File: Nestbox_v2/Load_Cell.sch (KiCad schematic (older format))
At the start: 33 parts, among them J601 LOAD_CELL_CONN_01X04, Q601 DMG2301L-7, Q602 DMG3402L, Q603 DMG2301L-7, Q604 DMG3402L, U601 ADS1220

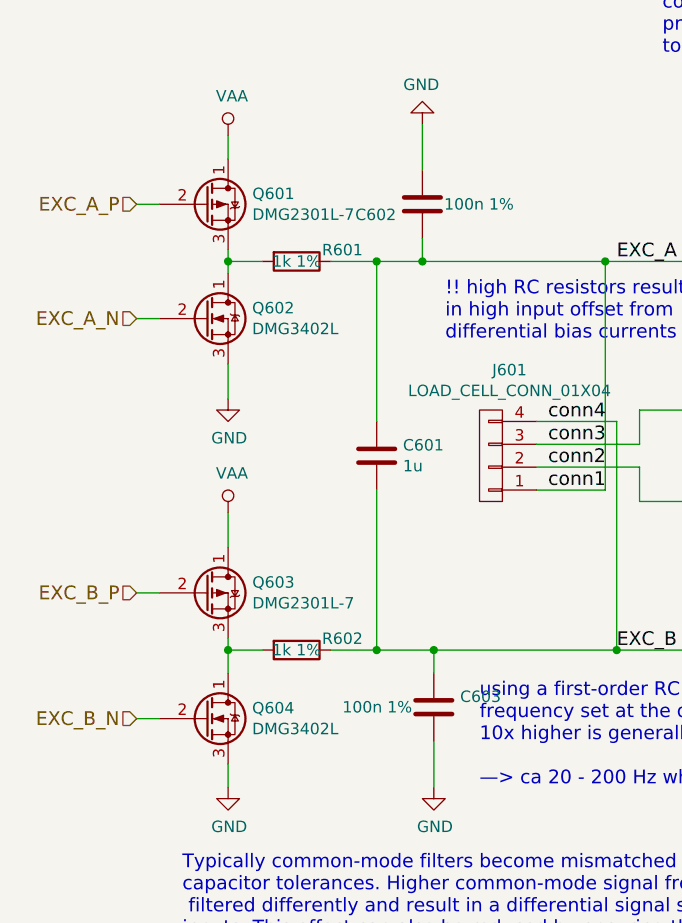
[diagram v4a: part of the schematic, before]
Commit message: corrected transistor pins
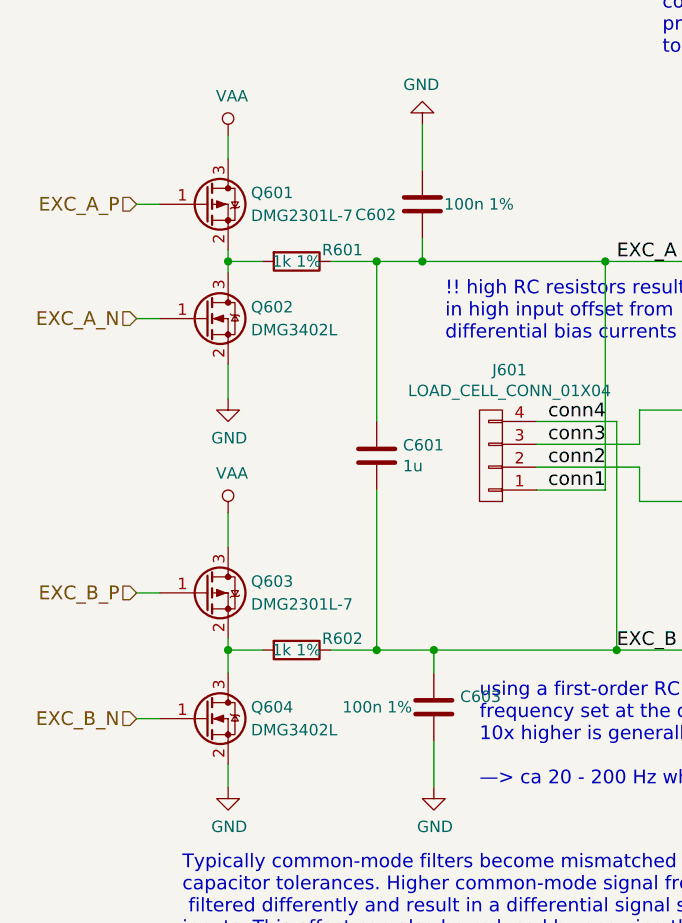
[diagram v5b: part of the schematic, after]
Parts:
- removed Q601, Q603: DMG2301L-7, TO_SOT_Packages_SMD:TSOT-23, symbol Q_PMOS_DGS
- removed Q602, Q604: DMG3402L, TO_SOT_Packages_SMD:TSOT-23, symbol Q_NMOS_DGS
- added Q601, Q603: DMG2301L-7, TO_SOT_Packages_SMD:TSOT-23, symbol Q_PMOS_GSD
- added Q602, Q604: DMG3402L, TO_SOT_Packages_SMD:TSOT-23, symbol Q_NMOS_GSD
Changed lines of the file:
@@
 $EndDescr
 $Comp
-L +3V3 #PWR051
+L +3V3 #PWR615
 U 1 1 5AF731D8
 P 7950 2900
-F 0 "#PWR051" H 7950 2750 50  0001 C CNN
+F 0 "#PWR615" H 7950 2750 50  0001 C CNN
 F 1 "+3V3" H 7965 3073 50  0000 C CNN
 F 2 "" H 7950 2900 50  0001 C CNN
@@
 $EndComp
 $Comp
-L GND #PWR052
+L GND #PWR616
 U 1 1 5AF734D9
 P 7950 4600
-F 0 "#PWR052" H 7950 4350 50  0001 C CNN
+F 0 "#PWR616" H 7950 4350 50  0001 C CNN
 F 1 "GND" H 7955 4427 50  0000 C CNN
 F 2 "" H 7950 4600 50  0001 C CNN
@@
 $EndComp
 $Comp
-L GND #PWR053
+L GND #PWR618
 U 1 1 5AF737C3
 P 8050 4600
-F 0 "#PWR053" H 8050 4350 50  0001 C CNN
+F 0 "#PWR618" H 8050 4350 50  0001 C CNN
 F 1 "GND" H 8055 4427 50  0000 C CNN
 F 2 "" H 8050 4600 50  0001 C CNN
@@
 $EndComp
 $Comp
-L GND #PWR054
+L GND #PWR619
 U 1 1 5AF737DA
 P 8650 3100
-F 0 "#PWR054" H 8650 2850 50  0001 C CNN
+F 0 "#PWR619" H 8650 2850 50  0001 C CNN
 F 1 "GND" V 8655 2972 50  0000 R CNN
 F 2 "" H 8650 3100 50  0001 C CNN
@@
 $EndComp
 $Comp
-L GND #PWR055
+L GND #PWR620
 U 1 1 5AF73803
 P 8650 3350
-F 0 "#PWR055" H 8650 3100 50  0001 C CNN
+F 0 "#PWR620" H 8650 3100 50  0001 C CNN
 F 1 "GND" V 8655 3222 50  0000 R CNN
 F 2 "" H 8650 3350 50  0001 C CNN
@@
 $EndComp
 $Comp
-L GND #PWR056
+L GND #PWR614
 U 1 1 5AF73B67
 P 7450 3400
-F 0 "#PWR056" H 7450 3150 50  0001 C CNN
+F 0 "#PWR614" H 7450 3150 50  0001 C CNN
 F 1 "GND" V 7455 3272 50  0000 R CNN
 F 2 "" H 7450 3400 50  0001 C CNN
@@
 $EndComp
 $Comp
-L GND #PWR057
+L GND #PWR613
 U 1 1 5AF73BBF
 P 7450 3100
-F 0 "#PWR057" H 7450 2850 50  0001 C CNN
+F 0 "#PWR613" H 7450 2850 50  0001 C CNN
 F 1 "GND" V 7455 2972 50  0000 R CNN
 F 2 "" H 7450 3100 50  0001 C CNN
@@
 $EndComp
 $Comp
-L GND #PWR058
+L GND #PWR610
 U 1 1 5AF756EC
 P 4400 4000
-F 0 "#PWR058" H 4400 3750 50  0001 C CNN
+F 0 "#PWR610" H 4400 3750 50  0001 C CNN
 F 1 "GND" H 4405 3827 50  0000 C CNN
 F 2 "" H 4400 4000 50  0001 C CNN
@@
 $EndComp
 $Comp
-L GND #PWR059
+L GND #PWR607
 U 1 1 5AF75761
 P 3900 4000
-F 0 "#PWR059" H 3900 3750 50  0001 C CNN
+F 0 "#PWR607" H 3900 3750 50  0001 C CNN
 F 1 "GND" H 3905 3827 50  0000 C CNN
 F 2 "" H 3900 4000 50  0001 C CNN
@@
 $EndComp
 $Comp
-L GND #PWR060
+L GND #PWR621
 U 1 1 5AF76892
 P 8800 4350
-F 0 "#PWR060" H 8800 4100 50  0001 C CNN
+F 0 "#PWR621" H 8800 4100 50  0001 C CNN
 F 1 "GND" H 8805 4177 50  0000 C CNN
 F 2 "" H 8800 4350 50  0001 C CNN
@@
 EXC_B
 $Comp
-L Q_NMOS_DGS Q602
-U 1 1 5AF89295
-P 1550 3400
-F 0 "Q602" H 1755 3446 50  0000 L CNN
-F 1 "DMG3402L" H 1755 3355 50  0000 L CNN
-F 2 "TO_SOT_Packages_SMD:TSOT-23" H 1750 3500 50  0001 C CNN
-F 3 "" H 1550 3400 50  0001 C CNN
-	1    1550 3400
-	1    0    0    -1
-$EndComp
-$Comp
-L Q_NMOS_DGS Q604
-U 1 1 5AF89446
-P 1550 5150
-F 0 "Q604" H 1755 5196 50  0000 L CNN
-F 1 "DMG3402L" H 1755 5105 50  0000 L CNN
-F 2 "TO_SOT_Packages_SMD:TSOT-23" H 1750 5250 50  0001 C CNN
-F 3 "" H 1550 5150 50  0001 C CNN
-	1    1550 5150
-	1    0    0    -1
-$EndComp
-$Comp
-L Q_PMOS_DGS Q603
-U 1 1 5AF89513
-P 1550 4600
-F 0 "Q603" H 1756 4646 50  0000 L CNN
-F 1 "DMG2301L-7" H 1756 4555 50  0000 L CNN
-F 2 "TO_SOT_Packages_SMD:TSOT-23" H 1750 4700 50  0001 C CNN
-F 3 "" H 1550 4600 50  0001 C CNN
-	1    1550 4600
-	1    0    0    -1
-$EndComp
-$Comp
-L Q_PMOS_DGS Q601
-U 1 1 5AF89674
-P 1550 2900
-F 0 "Q601" H 1756 2946 50  0000 L CNN
-F 1 "DMG2301L-7" H 1756 2855 50  0000 L CNN
-F 2 "TO_SOT_Packages_SMD:TSOT-23" H 1750 3000 50  0001 C CNN
-F 3 "" H 1550 2900 50  0001 C CNN
-	1    1550 2900
-	1    0    0    -1
-$EndComp
-$Comp
-L GND #PWR061
+L GND #PWR602
 U 1 1 5AF8B9E6
 P 1650 3750
-F 0 "#PWR061" H 1650 3500 50  0001 C CNN
+F 0 "#PWR602" H 1650 3500 50  0001 C CNN
 F 1 "GND" H 1655 3577 50  0000 C CNN
 F 2 "" H 1650 3750 50  0001 C CNN
@@
 $EndComp
 $Comp
-L GND #PWR062
+L GND #PWR604
 U 1 1 5AF8BA1F
 P 1650 5450
-F 0 "#PWR062" H 1650 5200 50  0001 C CNN
+F 0 "#PWR604" H 1650 5200 50  0001 C CNN
 F 1 "GND" H 1655 5277 50  0000 C CNN
 F 2 "" H 1650 5450 50  0001 C CNN
@@
 $EndComp
 $Comp
-L VAA #PWR063
+L VAA #PWR601
 U 1 1 5AF8BE8C
 P 1650 2600
-F 0 "#PWR063" H 1650 2450 50  0001 C CNN
+F 0 "#PWR601" H 1650 2450 50  0001 C CNN
 F 1 "VAA" H 1667 2773 50  0000 C CNN
 F 2 "" H 1650 2600 50  0001 C CNN
@@
 $EndComp
 $Comp
-L VAA #PWR064
+L VAA #PWR603
 U 1 1 5AF8C0F0
 P 1650 4250
-F 0 "#PWR064" H 1650 4100 50  0001 C CNN
+F 0 "#PWR603" H 1650 4100 50  0001 C CNN
 F 1 "VAA" H 1667 4423 50  0000 C CNN
 F 2 "" H 1650 4250 50  0001 C CNN
@@
 $EndComp
 $Comp
-L VAA #PWR065
+L VAA #PWR617
 U 1 1 5AF8C129
 P 8050 2550
-F 0 "#PWR065" H 8050 2400 50  0001 C CNN
+F 0 "#PWR617" H 8050 2400 50  0001 C CNN
 F 1 "VAA" H 8067 2723 50  0000 C CNN
 F 2 "" H 8050 2550 50  0001 C CNN
@@
 $EndComp
 $Comp
-L GND #PWR066
+L GND #PWR606
 U 1 1 5AF8D573
 P 2550 5450
-F 0 "#PWR066" H 2550 5200 50  0001 C CNN
+F 0 "#PWR606" H 2550 5200 50  0001 C CNN
 F 1 "GND" H 2555 5277 50  0000 C CNN
 F 2 "" H 2550 5450 50  0001 C CNN
@@
 $EndComp
 $Comp
-L GND #PWR067
+L GND #PWR605
 U 1 1 5AF8D7AF
 P 2500 2550
-F 0 "#PWR067" H 2500 2300 50  0001 C CNN
+F 0 "#PWR605" H 2500 2300 50  0001 C CNN
 F 1 "GND" H 2505 2377 50  0000 C CNN
 F 2 "" H 2500 2550 50  0001 C CNN
@@
 $EndComp
 $Comp
-L GND #PWR068
+L GND #PWR612
 U 1 1 5AF97D06
 P 6100 4000
-F 0 "#PWR068" H 6100 3750 50  0001 C CNN
+F 0 "#PWR612" H 6100 3750 50  0001 C CNN
 F 1 "GND" H 6105 3827 50  0000 C CNN
 F 2 "" H 6100 4000 50  0001 C CNN
@@
 $EndComp
 $Comp
-L GND #PWR069
+L GND #PWR611
 U 1 1 5AF97F53
 P 5600 4000
-F 0 "#PWR069" H 5600 3750 50  0001 C CNN
+F 0 "#PWR611" H 5600 3750 50  0001 C CNN
 F 1 "GND" H 5605 3827 50  0000 C CNN
 F 2 "" H 5600 4000 50  0001 C CNN
@@
 LIGHTBARRIER_LED_OUTPUT
 $Comp
-L +3.3V #PWR070
+L +3.3V #PWR608
 U 1 1 5B145174
 P 3950 6750
-F 0 "#PWR070" H 3950 6600 50  0001 C CNN
+F 0 "#PWR608" H 3950 6600 50  0001 C CNN
 F 1 "+3.3V" H 3950 6890 50  0000 C CNN
 F 2 "" H 3950 6750 50  0001 C CNN
@@
 $EndComp
 $Comp
-L GND #PWR071
+L GND #PWR609
 U 1 1 5B14520C
 P 3950 7050
-F 0 "#PWR071" H 3950 6800 50  0001 C CNN
+F 0 "#PWR609" H 3950 6800 50  0001 C CNN
 F 1 "GND" H 3950 6900 50  0000 C CNN
 F 2 "" H 3950 7050 50  0001 C CNN
@@
 Wire Wire Line
 	3300 4150 3300 3150
+$Comp
+L Q_PMOS_GSD Q603
+U 1 1 5B188D68
+P 1550 4600
+F 0 "Q603" H 1750 4650 50  0000 L CNN
+F 1 "DMG2301L-7" H 1750 4550 50  0000 L CNN
+F 2 "TO_SOT_Packages_SMD:TSOT-23" H 1750 4700 50  0001 C CNN
+F 3 "" H 1550 4600 50  0001 C CNN
+	1    1550 4600
+	1    0    0    -1
+$EndComp
+$Comp
+L Q_PMOS_GSD Q601
+U 1 1 5B1892D4
+P 1550 2900
+F 0 "Q601" H 1750 2950 50  0000 L CNN
+F 1 "DMG2301L-7" H 1750 2850 50  0000 L CNN
+F 2 "TO_SOT_Packages_SMD:TSOT-23" H 1750 3000 50  0001 C CNN
+F 3 "" H 1550 2900 50  0001 C CNN
+	1    1550 2900
+	1    0    0    -1
+$EndComp
+$Comp
+L Q_NMOS_GSD Q602
+U 1 1 5B1899A1
+P 1550 3400
+F 0 "Q602" H 1750 3450 50  0000 L CNN
+F 1 "DMG3402L" H 1750 3350 50  0000 L CNN
+F 2 "TO_SOT_Packages_SMD:TSOT-23" H 1750 3500 50  0001 C CNN
+F 3 "" H 1550 3400 50  0001 C CNN
+	1    1550 3400
+	1    0    0    -1
+$EndComp
+$Comp
+L Q_NMOS_GSD Q604
+U 1 1 5B189ECC
+P 1550 5150
+F 0 "Q604" H 1750 5200 50  0000 L CNN
+F 1 "DMG3402L" H 1750 5100 50  0000 L CNN
+F 2 "TO_SOT_Packages_SMD:TSOT-23" H 1750 5250 50  0001 C CNN
+F 3 "" H 1550 5150 50  0001 C CNN
+	1    1550 5150
+	1    0    0    -1
+$EndComp
 $EndSCHEMATC

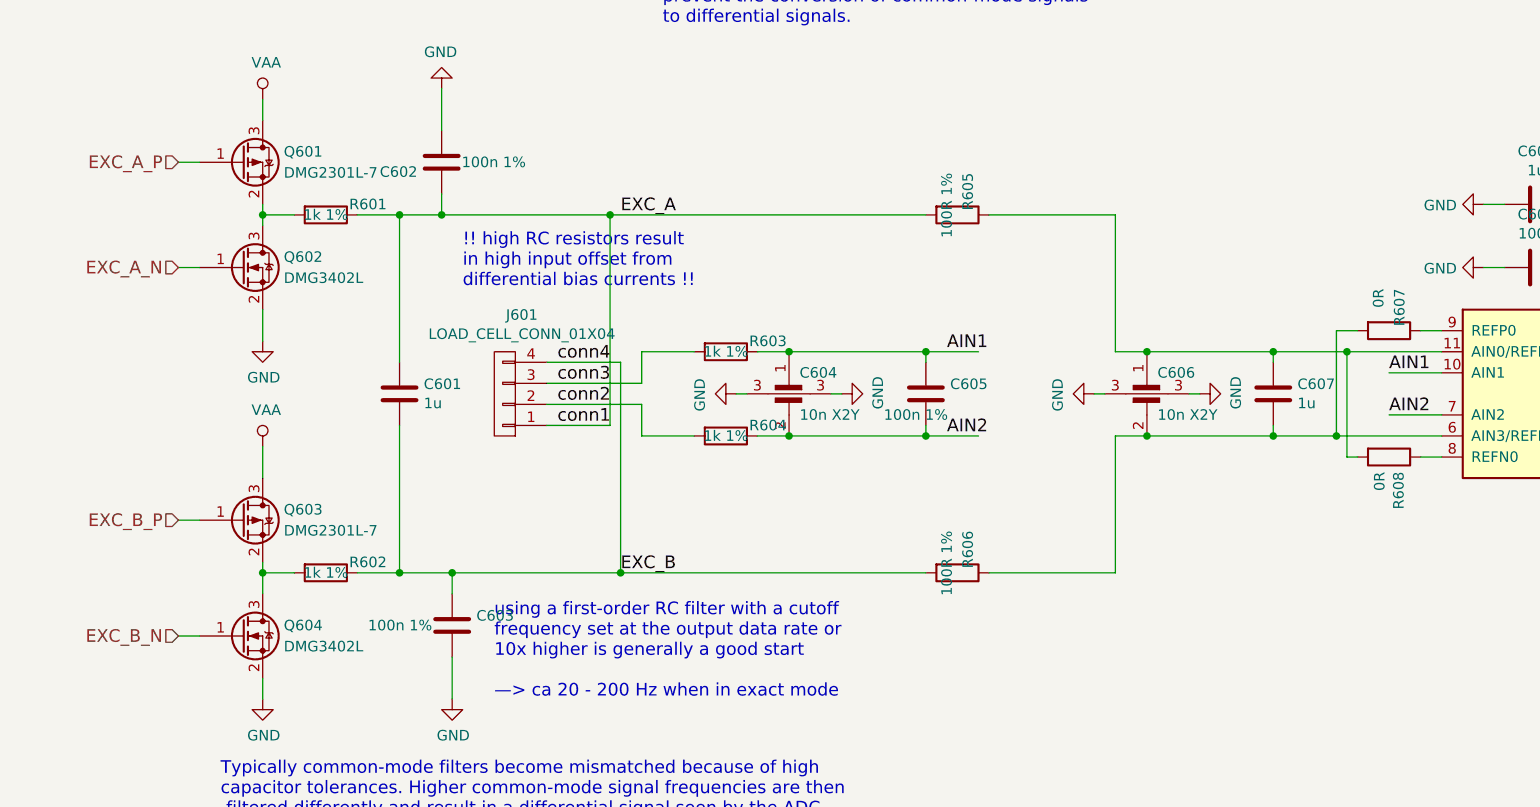
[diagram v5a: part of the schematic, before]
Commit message: annotated schematic with necessary changes to load cell circuit. added pull-ups for enable PMOSes
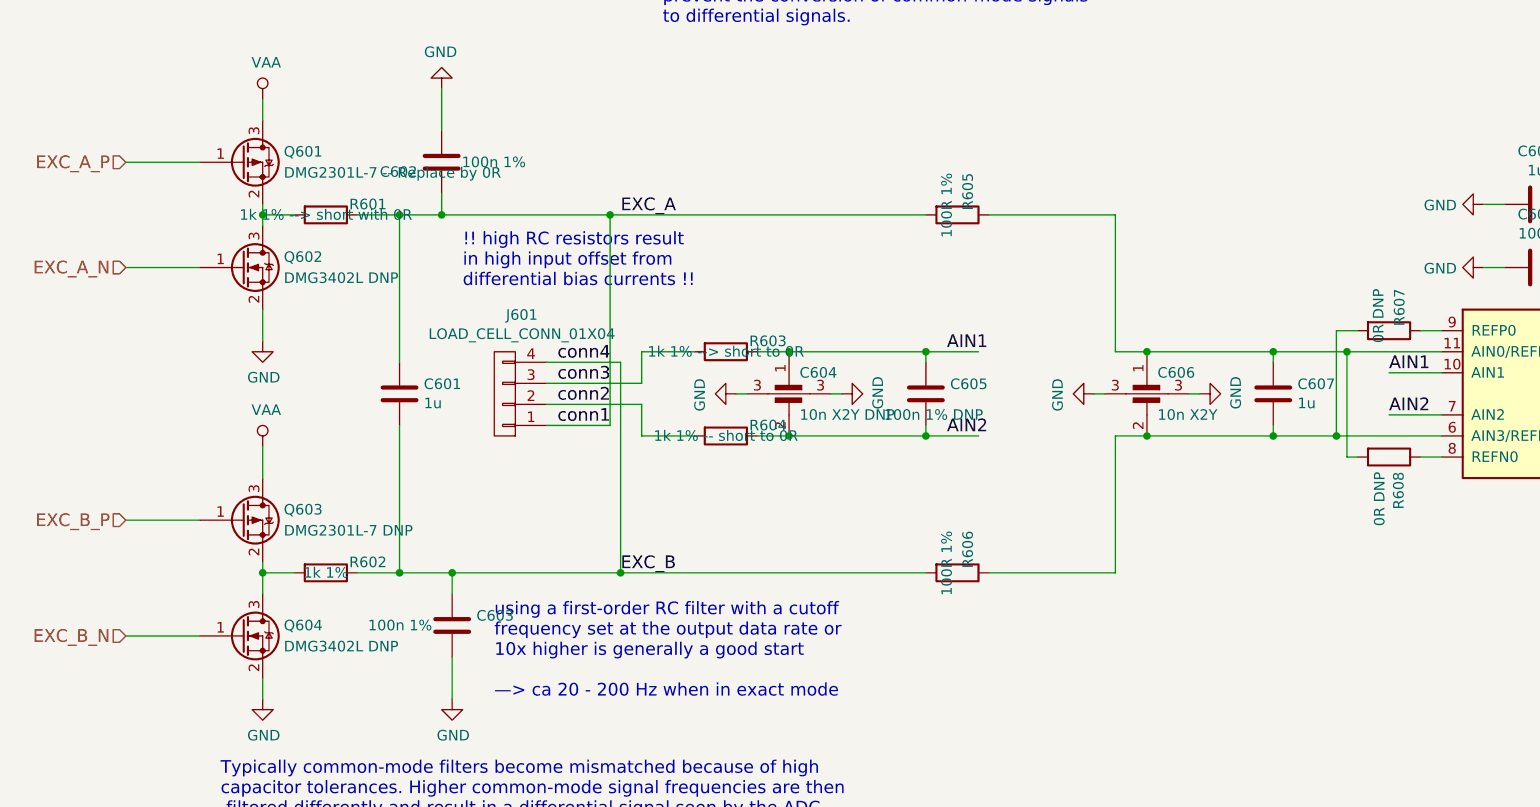
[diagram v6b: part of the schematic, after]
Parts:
- C604: value 10n X2Y -> 10n X2Y DNP
- C605: value 100n 1% -> 100n 1% DNP
- Q601: value DMG2301L-7 -> DMG2301L-7 -- Replace by 0R
- Q602, Q604: value DMG3402L -> DMG3402L DNP
- Q603: value DMG2301L-7 -> DMG2301L-7 DNP
- R601: value 1k 1% -> 1k 1% --> short with 0R
- R603: value 1k 1% -> 1k 1% --> short to 0R
- R604: value 1k 1% -> 1k 1% -- short to 0R
- R607, R608: value 0R -> 0R DNP
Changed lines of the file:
@@
 P 4800 4000
 F 0 "C605" H 4915 4046 50  0000 L CNN
-F 1 "100n 1%" H 4600 3900 50  0000 L CNN
+F 1 "100n 1% DNP" H 4600 3900 50  0000 L CNN
 F 2 "Capacitors_SMD:C_0603" H 4838 3850 50  0001 C CNN
 F 3 "" H 4800 4000 50  0001 C CNN
@@
 P 3850 3800
 F 0 "R603" V 3800 4000 50  0000 C CNN
-F 1 "1k 1%" V 3850 3800 50  0000 C CNN
+F 1 "1k 1% --> short to 0R" V 3850 3800 50  0000 C CNN
 F 2 "Resistors_SMD:R_0603" V 3780 3800 50  0001 C CNN
 F 3 "" H 3850 3800 50  0001 C CNN
@@
 P 3850 4200
 F 0 "R604" V 3800 4400 50  0000 C CNN
-F 1 "1k 1%" V 3850 4200 50  0000 C CNN
+F 1 "1k 1% -- short to 0R" V 3850 4200 50  0000 C CNN
 F 2 "Resistors_SMD:R_0603" V 3780 4200 50  0001 C CNN
 F 3 "" H 3850 4200 50  0001 C CNN
@@
 P 1950 3150
 F 0 "R601" V 1900 3350 50  0000 C CNN
-F 1 "1k 1%" V 1950 3150 50  0000 C CNN
+F 1 "1k 1% --> short with 0R" V 1950 3150 50  0000 C CNN
 F 2 "Resistors_SMD:R_0603" V 1880 3150 50  0001 C CNN
 F 3 "" H 1950 3150 50  0001 C CNN
@@
 P 7000 4300
 F 0 "R608" H 7070 4346 50  0000 L CNN
-F 1 "0R" H 7070 4255 50  0000 L CNN
+F 1 "0R DNP" H 7070 4255 50  0000 L CNN
 F 2 "Resistors_SMD:R_0603" V 6930 4300 50  0001 C CNN
 F 3 "" H 7000 4300 50  0001 C CNN
@@
 P 7000 3700
 F 0 "R607" H 6800 3750 50  0000 L CNN
-F 1 "0R" H 6800 3650 50  0000 L CNN
+F 1 "0R DNP" H 6800 3650 50  0000 L CNN
 F 2 "Resistors_SMD:R_0603" V 6930 3700 50  0001 C CNN
 F 3 "" H 7000 3700 50  0001 C CNN
@@
 P 4150 4100
 F 0 "C604" H 4200 4300 50  0000 L CNN
-F 1 "10n X2Y" H 4200 4100 50  0000 L CNN
+F 1 "10n X2Y DNP" H 4200 4100 50  0000 L CNN
 F 2 "Octanis3:Capacitor_X2Y_603" V 4150 4100 50  0001 C CNN
 F 3 "" V 4150 4100 50  0001 C CNN
@@
 Connection ~ 5850 4200
 Wire Wire Line
-	1250 3400 1350 3400
-Wire Wire Line
-	1250 2900 1350 2900
-Wire Wire Line
-	1250 4600 1350 4600
-Wire Wire Line
-	1250 5150 1350 5150
+	1000 3400 1350 3400
+Wire Wire Line
+	1000 2900 1350 2900
+Wire Wire Line
+	1000 4600 1350 4600
+Wire Wire Line
+	1000 5150 1350 5150
 Text HLabel 9750 3700 2    60   Input ~ 0
 SPI_SCK
@@
 Text HLabel 9750 4200 2    60   Input ~ 0
 DRDY_N
-Text HLabel 1250 2900 0    60   Input ~ 0
+Text HLabel 1000 2900 0    60   Input ~ 0
 EXC_A_P
-Text HLabel 1250 3400 0    60   Input ~ 0
+Text HLabel 1000 3400 0    60   Input ~ 0
 EXC_A_N
-Text HLabel 1250 5150 0    60   Input ~ 0
+Text HLabel 1000 5150 0    60   Input ~ 0
 EXC_B_N
-Text HLabel 1250 4600 0    60   Input ~ 0
+Text HLabel 1000 4600 0    60   Input ~ 0
 EXC_B_P
 Text Label 3050 4150 0    60   ~ 0
@@
 P 1550 4600
 F 0 "Q603" H 1750 4650 50  0000 L CNN
-F 1 "DMG2301L-7" H 1750 4550 50  0000 L CNN
+F 1 "DMG2301L-7 DNP" H 1750 4550 50  0000 L CNN
 F 2 "TO_SOT_Packages_SMD:TSOT-23" H 1750 4700 50  0001 C CNN
 F 3 "" H 1550 4600 50  0001 C CNN
@@
 P 1550 2900
 F 0 "Q601" H 1750 2950 50  0000 L CNN
-F 1 "DMG2301L-7" H 1750 2850 50  0000 L CNN
+F 1 "DMG2301L-7 -- Replace by 0R" H 1750 2850 50  0000 L CNN
 F 2 "TO_SOT_Packages_SMD:TSOT-23" H 1750 3000 50  0001 C CNN
 F 3 "" H 1550 2900 50  0001 C CNN
@@
 P 1550 3400
 F 0 "Q602" H 1750 3450 50  0000 L CNN
-F 1 "DMG3402L" H 1750 3350 50  0000 L CNN
+F 1 "DMG3402L DNP" H 1750 3350 50  0000 L CNN
 F 2 "TO_SOT_Packages_SMD:TSOT-23" H 1750 3500 50  0001 C CNN
 F 3 "" H 1550 3400 50  0001 C CNN
@@
 P 1550 5150
 F 0 "Q604" H 1750 5200 50  0000 L CNN
-F 1 "DMG3402L" H 1750 5100 50  0000 L CNN
+F 1 "DMG3402L DNP" H 1750 5100 50  0000 L CNN
 F 2 "TO_SOT_Packages_SMD:TSOT-23" H 1750 5250 50  0001 C CNN
 F 3 "" H 1550 5150 50  0001 C CNN
